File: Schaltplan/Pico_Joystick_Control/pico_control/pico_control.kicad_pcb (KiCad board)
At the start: 2 copper layers, 7 parts, among them J1 RJ45, J3 RJ12, U1 TXB0104D, U2 TBA1-1211

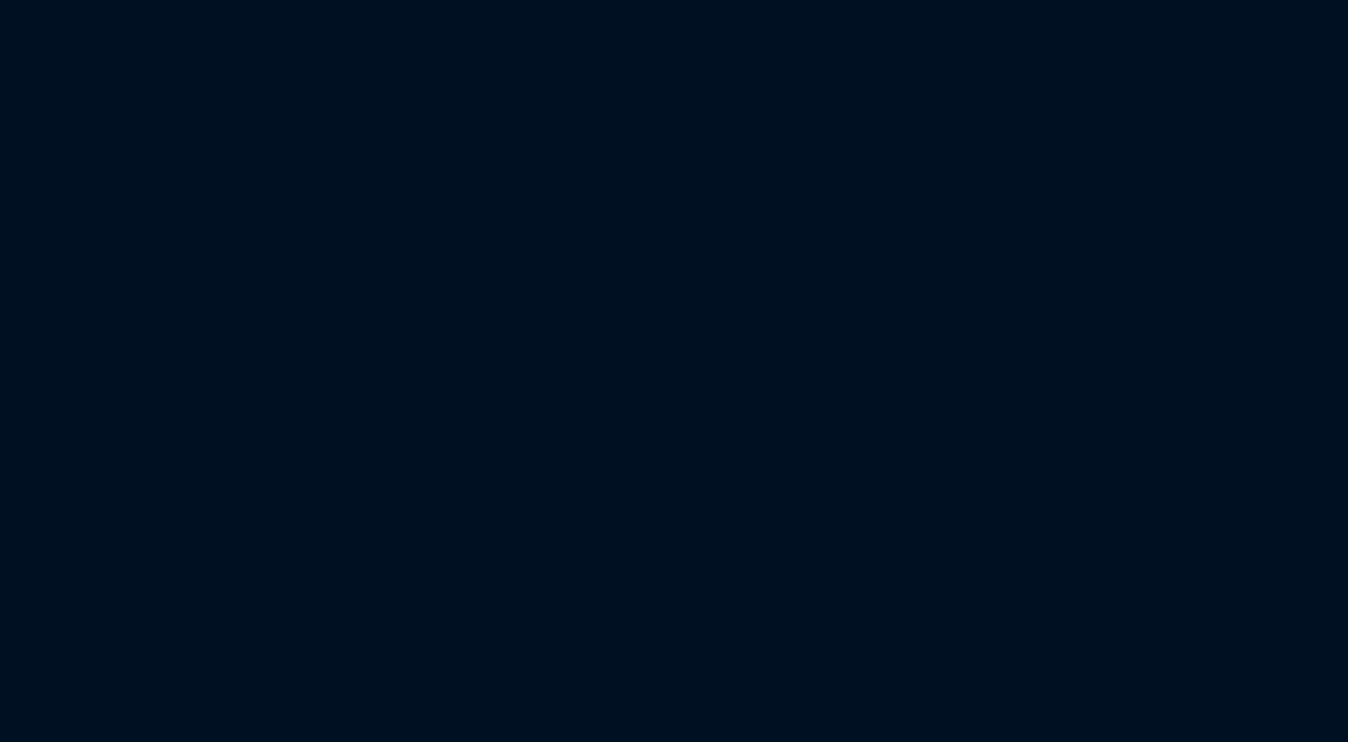
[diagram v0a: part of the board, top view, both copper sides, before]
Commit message: rpi zero addad to scheme
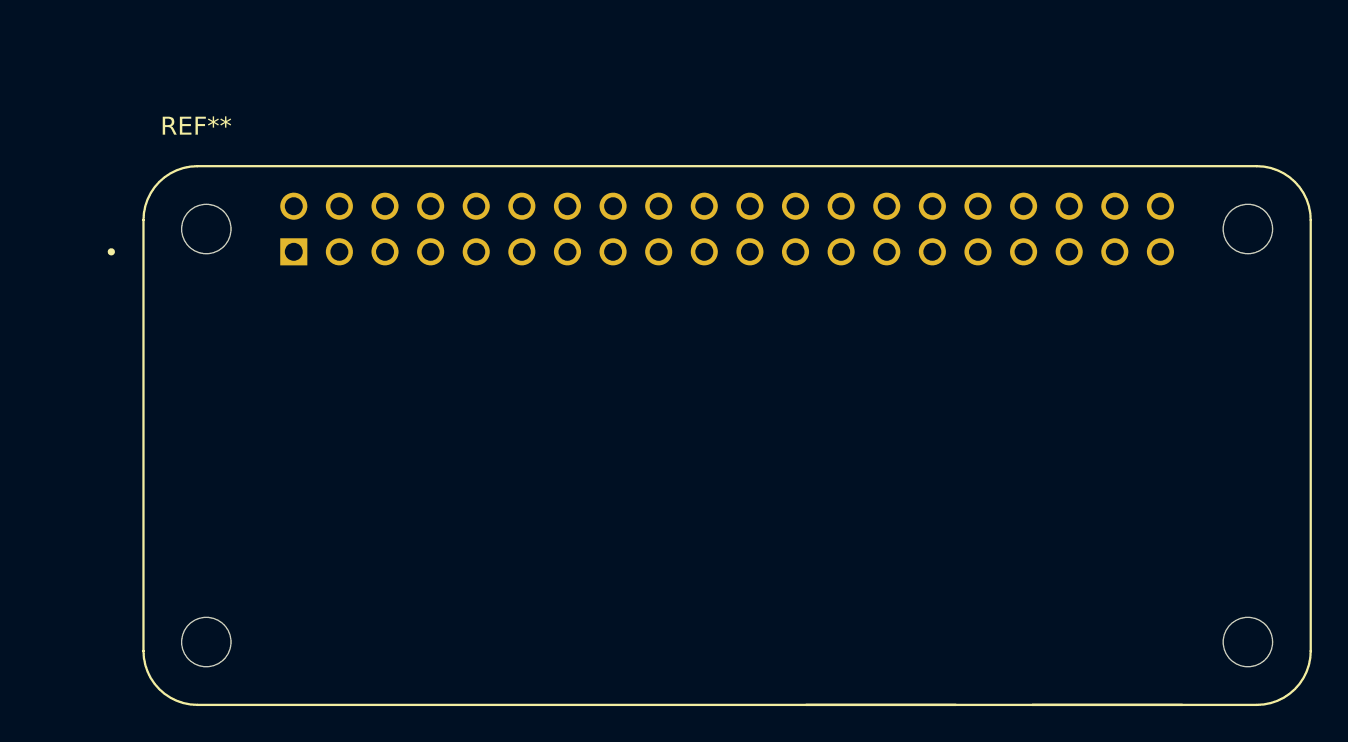
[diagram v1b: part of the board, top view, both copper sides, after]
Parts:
- added REF**: MODULE_RASPBERRY_PI_ZERO_2_W, RASPBERRY_PI_ZERO_2_W:MODULE_RASPBERRY_PI_ZERO_2_W, F.Cu at (181.5, 99.5)
